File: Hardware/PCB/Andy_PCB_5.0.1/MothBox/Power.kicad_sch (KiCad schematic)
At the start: 25 parts, among them P1 Raw Input, P2 Input to regulator, P3 12V Regulated Input, Q1 BC817, Q2 SUD50P06-15-GE3, U1 Place Holder voltage regulator, U2 XL4015E1, U3 INA219BIDCNT

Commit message: days updates - schematic cleanups
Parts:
- F1: value Polyfuse -> 5A
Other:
- moved on the sheet: F1
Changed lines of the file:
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@@
 	(text "Current and Voltage measurement\n"
 		(exclude_from_sim no)
-		(at 201.422 18.288 0)
+		(at 201.168 16.002 0)
 		(effects
 			(font
@@
 	)
 	(junction
-		(at 52.07 73.66)
-		(diameter 0)
-		(color 0 0 0 0)
-	)
-	(junction
 		(at 71.12 110.49)
 		(diameter 0)
@@
 	(wire
 		(pts
+			(xy 172.72 121.92) (xy 172.72 123.19)
+		)
+		(stroke
+			(width 0)
+			(type default)
+		)
+	)
+	(wire
+		(pts
 			(xy 124.46 53.34) (xy 124.46 55.88)
 		)
@@
 	(wire
 		(pts
-			(xy 52.07 67.31) (xy 52.07 73.66)
+			(xy 87.63 113.03) (xy 87.63 115.57)
 		)
 		(stroke
@@
 	(wire
 		(pts
-			(xy 87.63 113.03) (xy 87.63 115.57)
+			(xy 113.03 139.7) (xy 113.03 142.24)
 		)
 		(stroke
@@
 	(wire
 		(pts
-			(xy 113.03 139.7) (xy 113.03 142.24)
+			(xy 64.77 123.19) (xy 71.12 123.19)
 		)
 		(stroke
@@
 	(wire
 		(pts
-			(xy 64.77 123.19) (xy 71.12 123.19)
+			(xy 124.46 59.69) (xy 124.46 55.88)
 		)
 		(stroke
@@
 	(wire
 		(pts
-			(xy 124.46 59.69) (xy 124.46 55.88)
+			(xy 110.49 139.7) (xy 113.03 139.7)
 		)
 		(stroke
@@
 	(wire
 		(pts
-			(xy 110.49 139.7) (xy 113.03 139.7)
+			(xy 110.49 119.38) (xy 110.49 107.95)
 		)
 		(stroke
@@
 	(wire
 		(pts
-			(xy 110.49 119.38) (xy 110.49 107.95)
+			(xy 52.07 67.31) (xy 52.07 73.66)
 		)
 		(stroke
@@
 	(wire
 		(pts
+			(xy 172.72 123.19) (xy 168.91 123.19)
+		)
+		(stroke
+			(width 0)
+			(type default)
+		)
+	)
+	(wire
+		(pts
 			(xy 189.23 55.88) (xy 189.23 57.15)
 		)
@@
 	(wire
 		(pts
-			(xy 63.5 19.05) (xy 63.5 73.66)
+			(xy 63.5 19.05) (xy 63.5 67.31)
 		)
 		(stroke
@@
 	(wire
 		(pts
-			(xy 52.07 73.66) (xy 53.34 73.66)
+			(xy 52.07 67.31) (xy 53.34 67.31)
 		)
 		(stroke
@@
 	)
 	(label "PWR_IN"
-		(at 52.07 66.04 0)
+		(at 52.07 73.66 0)
 		(effects
 			(font
@@
 	)
 	(symbol
+		(lib_id "MB_Library:PWR_FLAG")
+		(at 172.72 121.92 0)
+		(unit 1)
+		(exclude_from_sim no)
+		(in_bom yes)
+		(on_board yes)
+		(dnp no)
+		(property "Reference" "#FLG03"
+			(at 172.72 120.015 0)
+			(effects
+				(font
+					(size 1.27 1.27)
+				)
+				(hide yes)
+			)
+		)
+		(property "Value" "PWR_FLAG"
+			(at 176.022 117.856 0)
+			(effects
+				(font
+					(size 1.27 1.27)
+				)
+			)
+		)
+		(property "Footprint" ""
+			(at 172.72 121.92 0)
+			(effects
+				(font
+					(size 1.27 1.27)
+				)
+				(hide yes)
+			)
+		)
+		(property "Datasheet" "~"
+			(at 172.72 121.92 0)
+			(effects
+				(font
+					(size 1.27 1.27)
+				)
+				(hide yes)
+			)
+		)
+		(property "Description" "Special symbol for telling ERC where power comes from"
+			(at 172.72 121.92 0)
+			(effects
+				(font
+					(size 1.27 1.27)
+				)
+				(hide yes)
+			)
+		)
+		(pin "1"
+		)
+		(instances
+			(project "MothBox"
+				(path "/9021e528-fc76-4423-a3f3-30f5652071cc/4a573100-9946-48c2-8ae5-35f893607623"
+					(reference "#FLG03")
+					(unit 1)
+				)
+			)
+		)
+	)
+	(symbol
 		(lib_id "MB_Library:+24V")
 		(at 52.07 63.5 0)
@@
 		)
 		(property "Value" "+5V"
-			(at 170.942 117.856 0)
+			(at 167.386 117.856 0)
 			(effects
 				(font
@@
 	(symbol
 		(lib_id "MB_Library:0805L010_60WR")
-		(at 58.42 73.66 180)
+		(at 58.42 67.31 180)
 		(unit 1)
 		(exclude_from_sim no)
@@
 		(on_board yes)
 		(dnp no)
-		(fields_autoplaced yes)
 		(property "Reference" "F1"
-			(at 58.42 67.31 0)
+			(at 58.928 64.77 0)
 			(effects
 				(font
@@
 			)
 		)
-		(property "Value" "Polyfuse"
-			(at 58.42 69.85 0)
+		(property "Value" "5A"
+			(at 58.42 70.104 0)
 			(effects
 				(font
@@
 		)
 		(property "Footprint" "easyeda2kicad:F0805"
-			(at 58.42 66.04 0)
+			(at 58.42 59.69 0)
 			(effects
 				(font
@@
 		)
 		(property "Datasheet" "~"
-			(at 58.42 73.66 0)
+			(at 58.42 67.31 0)
 			(effects
 				(font
@@
 		)
 		(property "Description" "Resettable fuse, polymeric positive temperature coefficient"
-			(at 58.42 73.66 0)
+			(at 58.42 67.31 0)
 			(effects
 				(font
@@
 		)
 		(property "LCSC Part no " ""
-			(at 58.42 73.66 0)
+			(at 58.42 67.31 0)
 			(effects
 				(font
@@
 		)
 		(property "LCSC PN" ""
-			(at 58.42 73.66 0)
+			(at 58.42 67.31 0)
 			(effects
 				(font
@@
 		)
 		(property "LCSC Part" "C22435897"
-			(at 58.42 63.5 0)
+			(at 58.42 57.15 0)
 			(effects
 				(font

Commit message: daily schematic updates
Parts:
- added Q11: YJQ10N2A, Pauls_Footprints:DFN2020-3, symbol _pauls_library:YJQ10N2A
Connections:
- new net: Q11.1 (D), Q11.2 (D), Q11.3 (D), Q11.5 (D), Q11.6 (D), Q11.8 (D)
- new net: Q11.4 (S), Q11.7 (S)
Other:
- note added: "Buck Convertor (Input <9V-36V> PWR to +5V)"
- note added: "External Buck/Boost 12 Volt Regulator"
- note added: "Up to 4A output at 5V"
- note removed: "Buck Convertor (Input PWR to +5V)"
- note removed: "PH: Up to 4A output at 5V"
- note removed: "PH: shouldn't this say 12V-36V? Will the regulator work below 12V?"
- moved on the sheet: C1, C2, C3, C4, C5, E1, L1, R2, R3, TP1, U2

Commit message: updated photo LEDs and the power page
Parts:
- removed F1: 5A, easyeda2kicad:F0805, symbol MB_Library:0805L010_60WR
- removed P1: Raw Input, easyeda2kicad:CONN-TH_2P-P5.08_DIBO_DB142R-5.08-2P, symbol MB_Library:DB142R-5.08-2P
- removed P2: Input to regulator, easyeda2kicad:CONN-TH_2P-P5.08_DIBO_DB142R-5.08-2P, symbol MB_Library:DB142R-5.08-2P
- removed P3: 12V Regulated Input, easyeda2kicad:CONN-TH_2P-P5.08_DIBO_DB142R-5.08-2P, symbol MB_Library:DB142R-5.08-2P
- removed Q1: BC817, Package_TO_SOT_SMD:SOT-23, symbol MB_Library:BC817_NPN_BJT
- removed Q11: YJQ10N2A, Pauls_Footprints:DFN2020-3, symbol _pauls_library:YJQ10N2A
- removed Q2: SUD50P06-15-GE3, easyeda2kicad:TO-252-3_L6.5-W5.8-P4.58-BL, symbol MB_Library:SUD50P06-15-GE3
- removed R1: 10k, Resistor_SMD:R_0805_2012Metric, symbol MB_Library:R_US
- removed TP2: VIN_-, TestPoint:TestPoint_THTPad_D1.0mm_Drill0.5mm, symbol MB_Library:TestPoint
- added D1: 10V, Diode_SMD:D_SOD-323, symbol Device:D_Zener_Small
- added F2: 6A trip, Resistor_SMD:R_1812_4532Metric, symbol Device:Polyfuse_Small
- added J1, J2, J3: DB141V-2.54-4P, easyeda2kicad:CONN-TH_4P-P2.54_DIBO_DB141V-2.54-4P, symbol Connector_Generic:Conn_01x04
- added Q1, Q8: JMTV210P02A, Pauls_Footprints:DFN2020-3, symbol _pauls_library:JMTV210P02A
- added Q2: BC817, Package_TO_SOT_SMD:SOT-23, symbol BC817:BC817_NPN_BJT
- added R29, R30: 10K, Resistor_SMD:R_0603_1608Metric, symbol MB_Library:R_Small
- added R31: 1K, Resistor_SMD:R_0603_1608Metric, symbol MB_Library:R_Small
- R4: value 0.1R/1% (PT2512FK-070R1L) -> 0.1R/1%
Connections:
- net +12V: now also J1.1 (Pin_1), J1.2 (Pin_2)
- net +24V: now also R4.1, U3.2 (IN-), Q1.2 (S), R30.1
- net EN_12VReg: now also R31.1
- net GND: now also J1.3 (Pin_3), J1.4 (Pin_4), J2.1 (Pin_1), J2.2 (Pin_2), Q2.2 (E), R29.2; no longer U1.2 (Vin-)
- net at U1.1 (Vin+): now also J3.3 (Pin_3), J3.4 (Pin_4), Q1.3 (D)
- net VIN+: no longer names the net of U3.1 (IN+)
- net VIN+: now also R4.2, F2.2; no longer R4.1
- removed net VIN-: R4.2, U3.2 (IN-)
- new net: J3.1 (Pin_1), J3.2 (Pin_2), U1.2 (Vin-)
- new net: D1.1 (K), F2.1, Q8.2 (S)
- new net: J2.3 (Pin_3), J2.4 (Pin_4), Q8.3 (D)
- new net: Q1.1 (G), Q2.3 (C), R30.2
- new net: D1.2 (A), Q8.1 (G), R29.1
- new net: Q2.1 (B), R31.2
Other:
- note added: "+"
- note added: "-"
- note added: "Basic Raw Input Voltage (9-36) Around 3A"
- note added: "Reverse Voltage Protection"
- note removed: "1) change MOSFET and cheaper to smaller type? 2) reverse S-D? 3) could change to a N-Mos and switch the GND line?"
- note removed: "Basic Raw Input Voltage (9-36) Around 2A"
- note removed: "C7500481 BSMD1812-300-24V 24V 3A 40A 6A 1812 Resettable Fuses ROHS"
- note removed: "PH: Andy, do you want current measurments testpoints?"
- note removed: "PH: Need to change the polyfuse to a physically larger size. the C22435897 trips at 0.3A"
- note removed: "PH: add in reverse polarity protection mosfet"
- company: (none) -> Digital Naturalism Laboritories
- title: (none) -> MothBox
- moved on the sheet: C6, U1, U3

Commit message: updated footprints and schematic
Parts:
- C1: symbol MB_Library:C_Polarized_Small_US -> MothBox_Symbol_Library:C_Polarized_Small_US; LCSC Part no  C90272 -> (none); LCSC_Part_No (none) -> C90272
- C2, C3, C5: symbol MB_Library:C_Small -> MothBox_Symbol_Library:C_Small; LCSC Part no  C3011704 -> (none); LCSC_Part_No (none) -> C3011704
- C4: symbol MB_Library:C_Polarized_Small_US -> MothBox_Symbol_Library:C_Polarized_Small_US; LCSC Part no  C2687701 -> (none); LCSC_Part_No (none) -> C2687701
- C6: symbol MB_Library:C_Small -> MothBox_Symbol_Library:C_Small
- D1: symbol Device:D_Zener_Small -> MothBox_Symbol_Library:D_Zener_Small
- E1: footprint easyeda2kicad:SMC_L6.9-W5.9-LS8.0-RD -> easyeda_footprints:SMC_L6.9-W5.9-LS8.0-RD; symbol MB_Library:SK54C_C5449119 -> MothBox_Symbol_Library:SK54C_C5449119; LCSC Part C5449119 -> (none); LCSC Part no  C5449119 -> (none); LCSC_Part (none) -> C5449119; LCSC_Part_No (none) -> C5449119
- F2: symbol Device:Polyfuse_Small -> MothBox_Symbol_Library:Polyfuse_Small
- J1, J2, J3: footprint easyeda2kicad:CONN-TH_4P-P2.54_DIBO_DB141V-2.54-4P -> easyeda_footprints:CONN-TH_4P-P2.54_DIBO_DB141V-2.54-4P; symbol Connector_Generic:Conn_01x04 -> MothBox_Symbol_Library:Conn_01x04
- L1: symbol MB_Library:L_Small -> MothBox_Symbol_Library:L_Small; LCSC Part no  C497913 -> (none); LCSC_Part_No (none) -> C497913
- Q1, Q8: symbol _pauls_library:JMTV210P02A -> MothBox_Symbol_Library:JMTV210P02A
- Q2: symbol BC817:BC817_NPN_BJT -> MothBox_Symbol_Library:BC817_NPN_BJT; LCSC Part no  C39828 -> (none); LCSC_Part_No (none) -> C39828
- R2: footprint Capacitor_SMD:C_0805_2012Metric_Pad1.18x1.45mm_HandSolder -> Resistor_SMD:R_0805_2012Metric; symbol MB_Library:R_Small -> MothBox_Symbol_Library:R_Small; LCSC Part no  C84376 -> (none); LCSC_Part_No (none) -> C84376
- R29, R30, R31: symbol MB_Library:R_Small -> MothBox_Symbol_Library:R_Small
- R3: footprint Capacitor_SMD:C_0805_2012Metric_Pad1.18x1.45mm_HandSolder -> Resistor_SMD:R_0805_2012Metric; symbol MB_Library:R_Small -> MothBox_Symbol_Library:R_Small; LCSC Part no  C114531 -> (none); LCSC_Part_No (none) -> C114531
- R4: footprint easyeda2kicad:R2512 -> Resistor_SMD:R_2512_6332Metric; symbol MB_Library:PCSR2512BR100M6 -> MothBox_Symbol_Library:PCSR2512BR100M6; LCSC Part C23067426 -> (none); LCSC_Part (none) -> C23067426
- R5: footprint easyeda2kicad:R0603 -> Resistor_SMD:R_0603_1608Metric; symbol MB_Library:FRC0603J103TS -> MothBox_Symbol_Library:FRC0603J103TS_1; LCSC Part C2930027 -> (none); LCSC_Part (none) -> C2930027
- R6: footprint easyeda2kicad:R0603 -> Resistor_SMD:R_0603_1608Metric; symbol MB_Library:FRC0603J103TS -> MothBox_Symbol_Library:FRC0603J103TS; LCSC Part C2930027 -> (none); LCSC_Part (none) -> C2930027
- TP1: symbol MB_Library:TestPoint -> MothBox_Symbol_Library:TestPoint
- U1: symbol MB_Library:Buck-Boost -> MothBox_Symbol_Library:Buck-Boost
- U2: footprint easyeda2kicad:TO-263-5_L10.2-W8.9-P1.70-TL -> easyeda_footprints:TO-263-5_L10.2-W8.9-P1.70-TL; symbol MB_Library:XL4015E1 -> MothBox_Symbol_Library:XL4015E1; LCSC Part C51661 -> (none); LCSC Part no  C51661 -> (none); LCSC_Part (none) -> C51661; LCSC_Part_No (none) -> C51661
- U3: footprint easyeda2kicad:SOT-23-8_L3.0-W1.7-P0.65-LS2.8-BR -> Package_TO_SOT_SMD:SOT-23-8; symbol MB_Library:INA219AIDCNR -> MothBox_Symbol_Library:INA219AIDCNR; LCSC Part C87469 -> (none); LCSC_Part (none) -> C87469

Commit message: daily PCB update
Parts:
- C1: footprint Capacitor_SMD:CP_Elec_10x12.5 -> MothBox_footprints_Library:CP_Elec_10x12.5
- C2, C3, C5: footprint Capacitor_SMD:C_0805_2012Metric_Pad1.18x1.45mm_HandSolder -> MothBox_footprints_Library:R_0603_1608Metric
- C4: footprint Capacitor_SMD:CP_Elec_10x10 -> MothBox_footprints_Library:CP_Elec_10x10
- C6: footprint Capacitor_SMD:C_0603_1608Metric -> MothBox_footprints_Library:C_0603_1608Metric; LCSC_Part_No (none) -> C3011704
- D1: footprint Diode_SMD:D_SOD-323 -> MothBox_footprints_Library:D_SOD-323
- E1: footprint easyeda_footprints:SMC_L6.9-W5.9-LS8.0-RD -> MothBox_footprints_Library:SMC_L6.9-W5.9-LS8.0-RD
- F2: footprint Resistor_SMD:R_1812_4532Metric -> Fuse:Fuse_1812_4532Metric
- J1, J2, J3: footprint easyeda_footprints:CONN-TH_4P-P2.54_DIBO_DB141V-2.54-4P -> MothBox_footprints_Library:CONN-TH_4P-P2.54_DIBO_DB141V-2.54-4P
- L1: footprint Inductor_SMD:L_Chilisin_BMRG00131360 -> MothBox_footprints_Library:L_Chilisin_BMRG00131360
- Q1, Q8: footprint Pauls_Footprints:DFN2020-3 -> MothBox_footprints_Library:DFN2020-3
- Q2: footprint Package_TO_SOT_SMD:SOT-23 -> MothBox_footprints_Library:SOT-23
- R2, R3: footprint Resistor_SMD:R_0805_2012Metric -> MothBox_footprints_Library:R_0805_2012Metric
- R29, R30, R31, R5, R6: footprint Resistor_SMD:R_0603_1608Metric -> MothBox_footprints_Library:R_0603_1608Metric
- R4: footprint Resistor_SMD:R_2512_6332Metric -> MothBox_footprints_Library:R_2512_6332Metric
- TP1: footprint TestPoint:TestPoint_THTPad_D1.0mm_Drill0.5mm -> MothBox_footprints_Library:TestPoint_THTPad_D1.0mm_Drill0.5mm
- U2: footprint easyeda_footprints:TO-263-5_L10.2-W8.9-P1.70-TL -> MothBox_footprints_Library:TO-263-5_L10.2-W8.9-P1.70-TL
- U3: footprint Package_TO_SOT_SMD:SOT-23-8 -> MothBox_footprints_Library:SOT-23-8

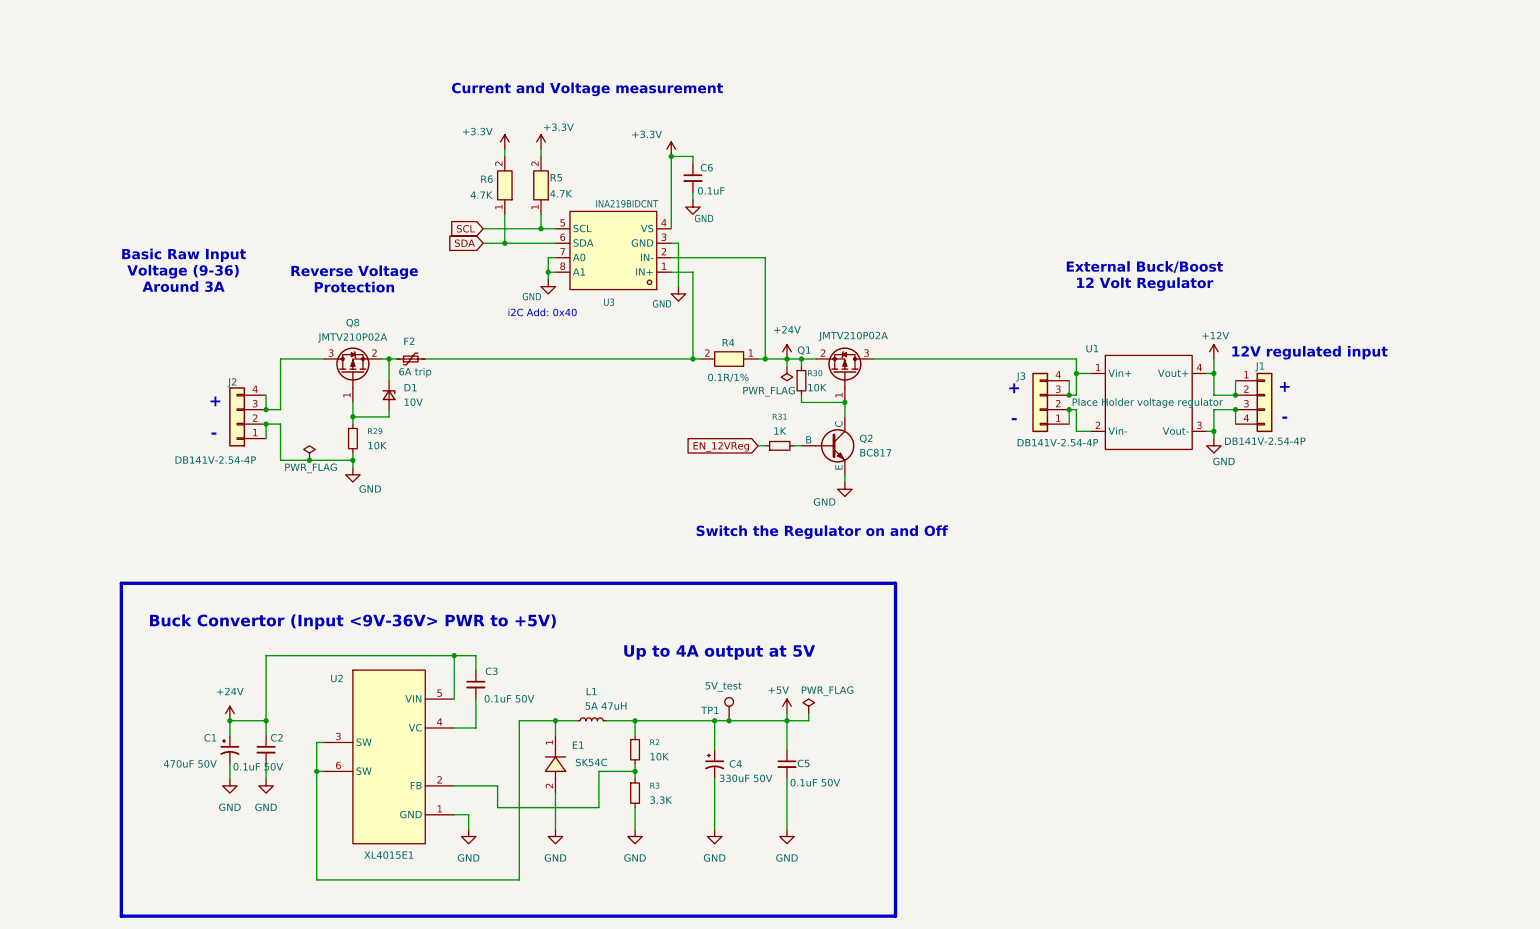
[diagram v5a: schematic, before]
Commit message: adding in datasheets
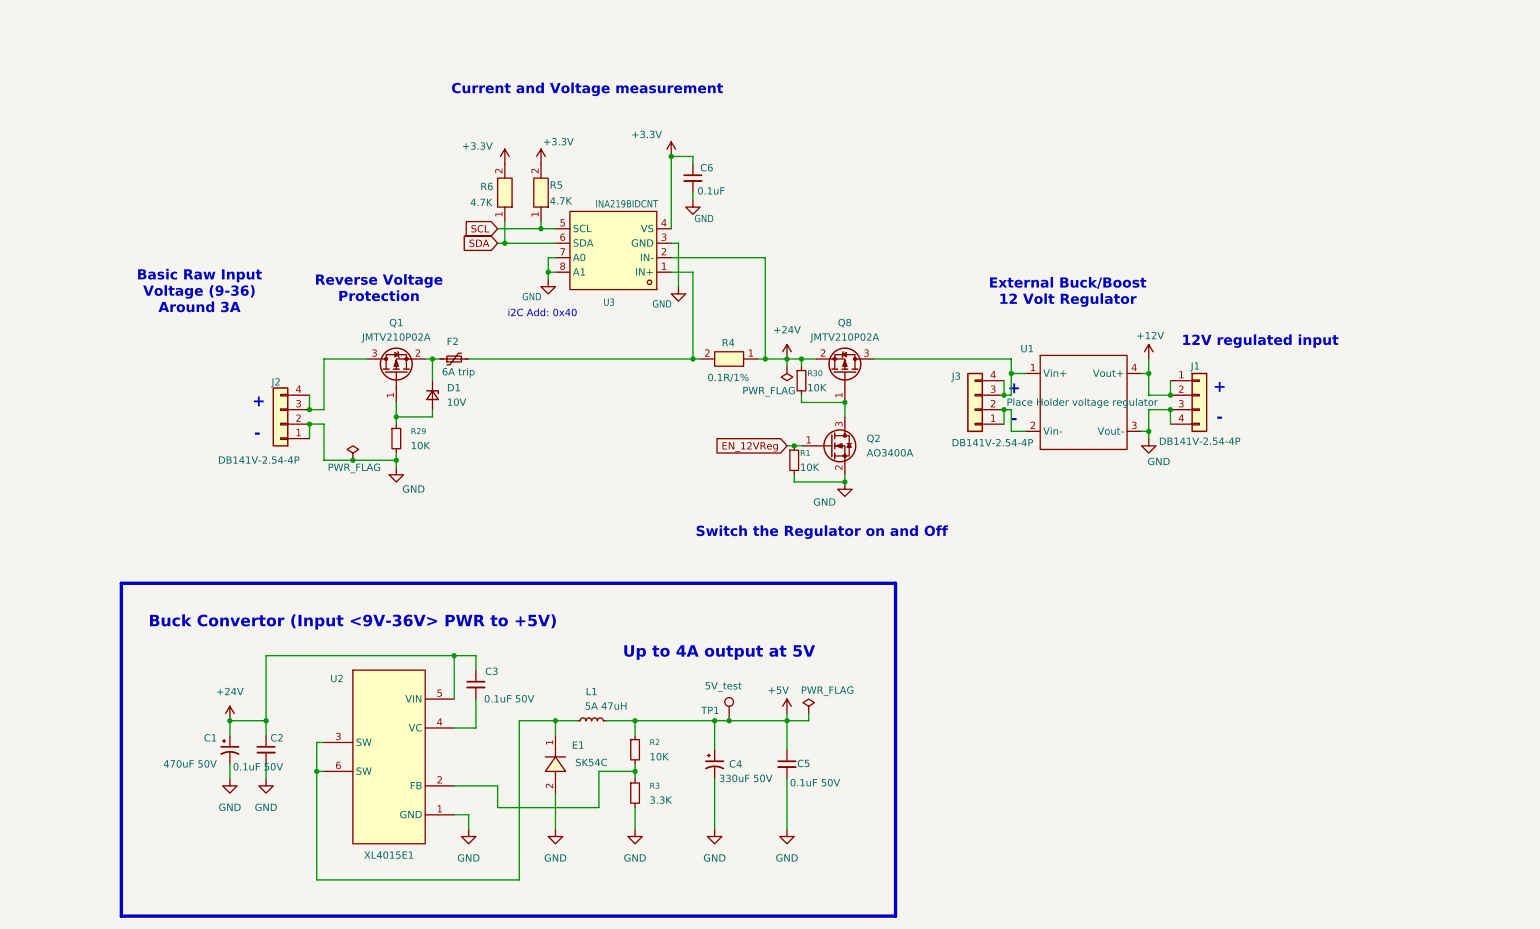
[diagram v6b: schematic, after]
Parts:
- removed Q2: BC817, MothBox_footprints_Library:SOT-23, symbol MothBox_Symbol_Library:BC817_NPN_BJT
- removed R31: 1K, MothBox_footprints_Library:R_0603_1608Metric, symbol MothBox_Symbol_Library:R_Small
- added Q2: AO3400A, MothBox_footprints_Library:SOT-23, symbol Transistor_FET:AO3400A
- added R1: 10K, MothBox_footprints_Library:R_0603_1608Metric, symbol MothBox_Symbol_Library:R_Small
- U2: footprint MothBox_footprints_Library:TO-263-5_L10.2-W8.9-P1.70-TL -> Package_TO_SOT_SMD:TO-263-5_TabPin3
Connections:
- net +24V: now also Q8.2 (S); no longer Q1.2 (S)
- net EN_12VReg: now also Q2.1 (G), R1.1
- net GND: now also Q2.2 (S), R1.2
- net at J3.3 (Pin_3), J3.4 (Pin_4), U1.1 (Vin+): now also Q8.3 (D); no longer Q1.3 (D)
- net at D1.1 (K), F2.1: now also Q1.2 (S); no longer Q8.2 (S)
- net at J2.3 (Pin_3), J2.4 (Pin_4): now also Q1.3 (D); no longer Q8.3 (D)
- net at Q1.1 (G): now also D1.2 (A), R29.1; no longer R30.2
- new net: Q2.3 (D), Q8.1 (G), R30.2
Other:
- moved on the sheet: D1, F2, J1, J2, J3, R29, R5, R6, U1

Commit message: rough outline of PCB. Lots of tidying up needed
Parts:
- added C8: 10uF, MothBox_footprints_Library:C_0603_1608Metric, symbol MothBox_Symbol_Library:C_Small
- added TP2: 24V_test, MothBox_footprints_Library:TestPoint_THTPad_D1.0mm_Drill0.5mm, symbol MothBox_Symbol_Library:TestPoint
- added TP5: 12V_test, MothBox_footprints_Library:TestPoint_THTPad_D1.0mm_Drill0.5mm, symbol MothBox_Symbol_Library:TestPoint
- Q1, Q8: footprint MothBox_footprints_Library:DFN2020-3 -> MothBox_footprints_Library:U-DFN2020-6_L2.0-W2.0-P0.65-BL
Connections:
- net +12V: now also TP5.1
- net +24V: now also Q8.4 (S), Q8.7 (S), TP2.1; no longer Q8.2 (S)
- net +3.3V: now also C8.1
- net GND: now also J3.1 (Pin_1), J3.2 (Pin_2), U1.2 (Vin-), C8.2
- net at J3.3 (Pin_3), J3.4 (Pin_4), U1.1 (Vin+): now also Q8.1 (D), Q8.2 (D), Q8.5 (D), Q8.6 (D), Q8.8 (D); no longer Q8.3 (D)
- net at D1.1 (K), F2.1: now also Q1.4 (S), Q1.7 (S); no longer Q1.2 (S)
- net at J2.3 (Pin_3), J2.4 (Pin_4): now also Q1.1 (D), Q1.2 (D), Q1.5 (D), Q1.6 (D), Q1.8 (D); no longer Q1.3 (D)
- net at D1.2 (A), R29.1: now also Q1.3 (G); no longer Q1.1 (G)
- net at Q2.3 (D), R30.2: now also Q8.3 (G); no longer Q8.1 (G)
